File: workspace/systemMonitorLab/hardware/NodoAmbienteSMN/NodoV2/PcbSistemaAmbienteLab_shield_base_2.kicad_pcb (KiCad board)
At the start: 2 copper layers, 53.6 x 67.9 mm, 19 parts, among them J1 Molex_MainBoard_DHT22, J2 Molex_MainBoard_BMP280, J3 Molex_MainBoard_Led_Status, J4 DC 5V, Q1 NPN, Q2 NPN, Q3 NPN, U1 NodeMcuEsp8266

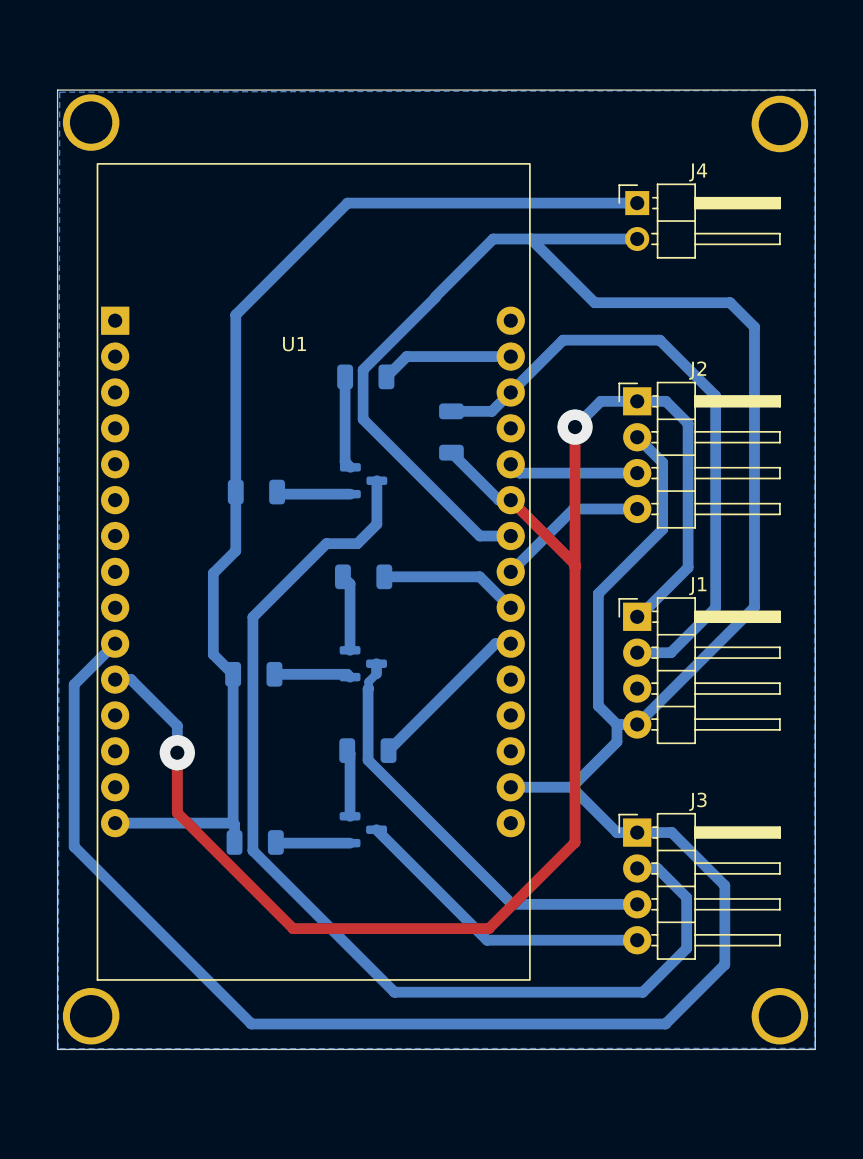
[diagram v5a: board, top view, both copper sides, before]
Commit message: Se termino de diseñar la version 2 del nodo ambiente, ahora se va a diseñar el case3d para que contenga al mismo
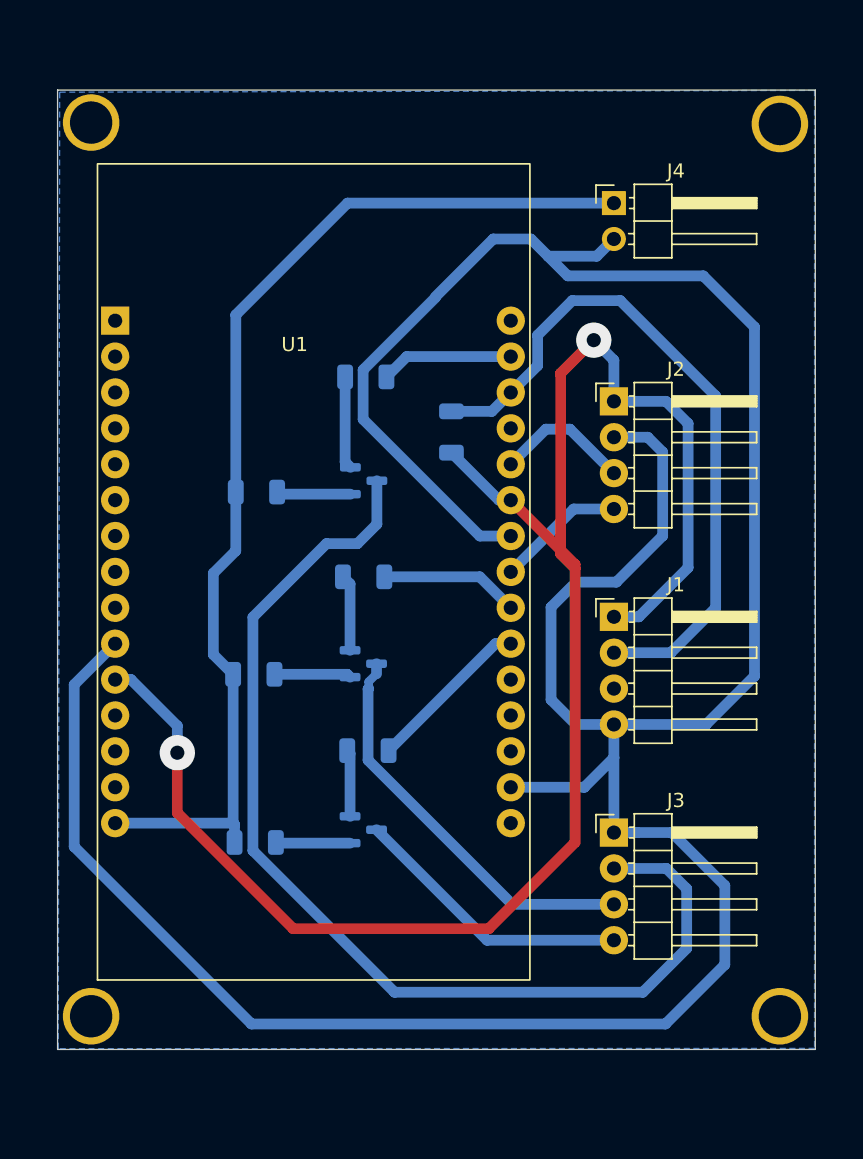
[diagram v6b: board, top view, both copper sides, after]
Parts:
- moved J1 1.65 mm to (156.2, 100.6)
- moved J2 1.65 mm to (156.2, 85.3)
- moved J3 1.65 mm to (156.2, 115.9)
- moved J4 1.65 mm to (156.2, 71.3)
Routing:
- net GND: track 214.1 -> 225.3 mm
- net 3V3: track 112.3 -> 122.9 mm
- net Net-(J1-Pin_2): track 44.3 -> 49.5 mm
- net Net-(J3-Pin_2): track 75.2 -> 77.2 mm
- net Net-(J3-Pin_3): track 30.4 -> 28.7 mm
- net Net-(J3-Pin_4): track 21.7 -> 20.0 mm
- net /shield_base/SDA: track 10.8 -> 9.14 mm
- net +5V: track 78.7 -> 77.0 mm

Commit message: Subo el resideño de los pcb's acorde al case 3d
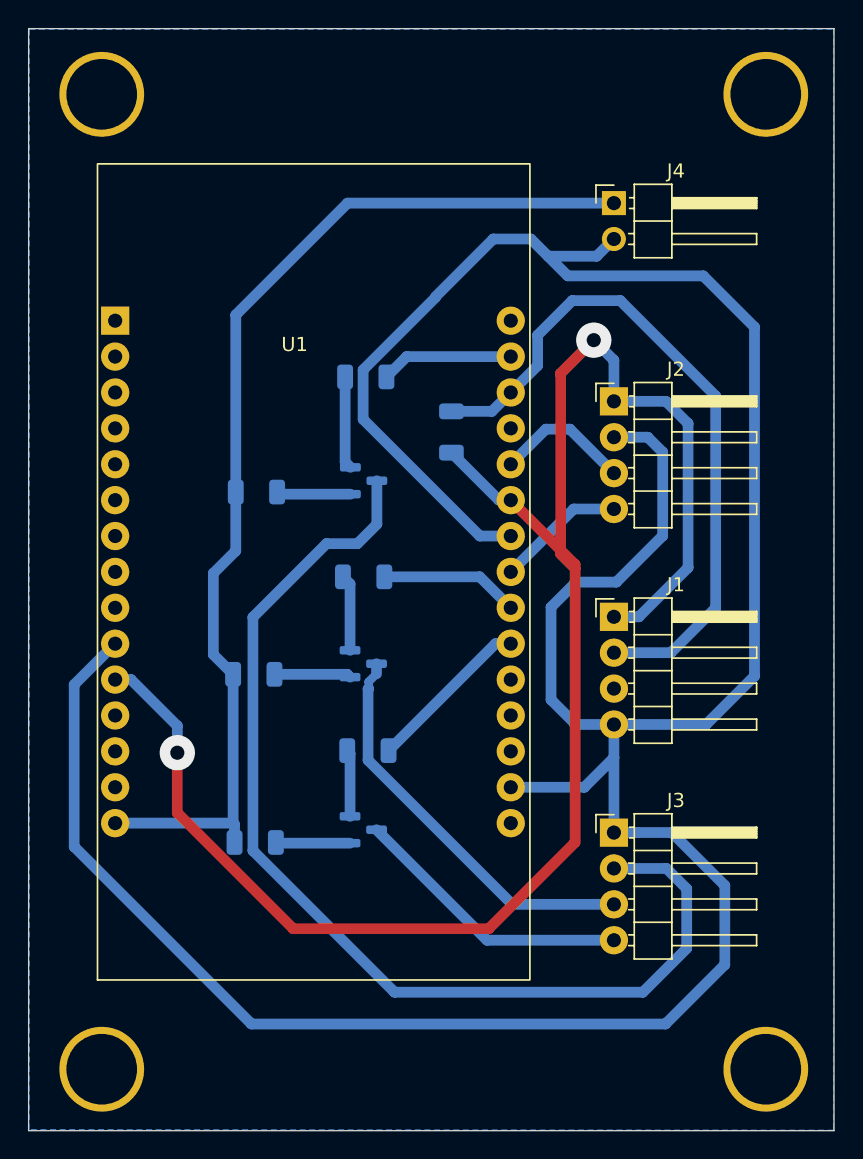
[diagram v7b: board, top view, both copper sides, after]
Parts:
- removed the ? at (117.3, 128.9)
- removed the ? at (168.1, 129.0)
- added ?: , , F.Cu at (121.1, 131.7)
- added ?: , , F.Cu at (168.1, 131.8)
- moved ? 1.41 mm to (167.1, 64.7)
- moved ? 1.00 mm to (118.2, 65.6)
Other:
- board size 53.6 x 67.9 mm -> 57 x 78 mm
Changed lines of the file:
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@@
 	(footprint ""
 		(layer "F.Cu")
-		(at 117.2 65.61)
+		(at 121.1 131.735)
 		(property "Reference" ""
 			(at 0 0 0)
@@
 		)
 		(pad "" thru_hole circle
-			(at 2 0 180)
-			(size 4 4)
-			(drill 3)
+			(at -1.15 0.875 180)
+			(size 6 6)
+			(drill 5)
+			(layers "*.Cu" "*.Mask")
+			(remove_unused_layers no)
+			(pinfunction "RV")
+			(pintype "bidirectional+no_connect")
+		)
+		(embedded_fonts no)
+	)
+	(footprint ""
+		(layer "F.Cu")
+		(at 118.2 65.61)
+		(property "Reference" ""
+			(at 0 0 0)
+			(layer "F.SilkS")
+			(effects
+				(font
+					(size 1.27 1.27)
+					(thickness 0.15)
+				)
+			)
+		)
+		(property "Value" ""
+			(at 0 0 0)
+			(layer "F.Fab")
+			(effects
+				(font
+					(size 1.27 1.27)
+					(thickness 0.15)
+				)
+			)
+		)
+		(property "Datasheet" ""
+			(at 0 0 0)
+			(layer "F.Fab")
+			(hide yes)
+			(effects
+				(font
+					(size 1.27 1.27)
+					(thickness 0.15)
+				)
+			)
+		)
+		(property "Description" ""
+			(at 0 0 0)
+			(layer "F.Fab")
+			(hide yes)
+			(effects
+				(font
+					(size 1.27 1.27)
+					(thickness 0.15)
+				)
+			)
+		)
+		(pad "" thru_hole circle
+			(at 1.75 -2 180)
+			(size 6 6)
+			(drill 5)
 			(layers "*.Cu" "*.Mask")
 			(remove_unused_layers no)
@@
 		(embedded_fonts no)
 	)
-	(footprint ""
-		(layer "F.Cu")
-		(at 117.3 128.86)
-		(property "Reference" ""
-			(at 0 0 0)
-			(layer "F.SilkS")
-			(effects
-				(font
-					(size 1.27 1.27)
-					(thickness 0.15)
-				)
-			)
-		)
-		(property "Value" ""
-			(at 0 0 0)
-			(layer "F.Fab")
-			(effects
-				(font
-					(size 1.27 1.27)
-					(thickness 0.15)
-				)
-			)
-		)
-		(property "Datasheet" ""
-			(at 0 0 0)
-			(layer "F.Fab")
-			(hide yes)
-			(effects
-				(font
-					(size 1.27 1.27)
-					(thickness 0.15)
-				)
-			)
-		)
-		(property "Description" ""
-			(at 0 0 0)
-			(layer "F.Fab")
-			(hide yes)
-			(effects
-				(font
-					(size 1.27 1.27)
-					(thickness 0.15)
-				)
-			)
-		)
-		(pad "" thru_hole circle
-			(at 1.9 0 180)
-			(size 4 4)
-			(drill 3)
-			(layers "*.Cu" "*.Mask")
-			(remove_unused_layers no)
-			(pinfunction "RV")
-			(pintype "bidirectional+no_connect")
-		)
-		(embedded_fonts no)
-	)
 	(footprint "Connector_PinHeader_2.54mm:PinHeader_1x04_P2.54mm_Horizontal"
 		(layer "F.Cu")
@@
 	(footprint ""
 		(layer "F.Cu")
-		(at 168.1 129.01)
+		(at 168.1 131.81)
 		(property "Reference" ""
 			(at 0 0 0)
@@
 		)
 		(pad "" thru_hole circle
-			(at -0.15 -0.15 180)
-			(size 4 4)
-			(drill 3)
+			(at -1.15 0.8 180)
+			(size 6 6)
+			(drill 5)
 			(layers "*.Cu" "*.Mask")
 			(remove_unused_layers no)
@@
 	(footprint ""
 		(layer "F.Cu")
-		(at 168.05 65.71 90)
+		(at 167.05 64.71 90)
 		(property "Reference" ""
 			(at 0 0 90)
@@
 		)
 		(pad "" thru_hole circle
-			(at 0 -0.1 270)
-			(size 4 4)
-			(drill 3)
+			(at 1.1 -0.1 270)
+			(size 6 6)
+			(drill 5)
 			(layers "*.Cu" "*.Mask")
 			(remove_unused_layers no)
@@
 	)
 	(gr_rect
-		(start 116.825 63.31)
-		(end 170.455 131.21)
+		(start 114.775 58.96)
+		(end 171.775 136.96)
 		(stroke
 			(width 0.05)
@@
 		(layer "Dwgs.User")
 		(pts
-			(xy 116.825 131.21) (xy 170.455 131.21)
+			(xy 171.775 58.96) (xy 171.775 136.96)
 		)
-		(height 4.8)
-		(orientation 0)
+		(height 18.48)
+		(orientation 1)
 		(format
 			(prefix "")
@@
 			(keep_text_aligned yes)
 		)
-		(gr_text "53.6300 mm"
-			(at 143.64 134.86 0)
+		(gr_text "78.0000 mm"
+			(at 189.105 97.96 90)
 			(layer "Dwgs.User")
 			(effects
@@
 		(layer "Dwgs.User")
 		(pts
-			(xy 170.45 63.36) (xy 170.35 131.21)
+			(xy 119.95 63.61) (xy 119.95 132.61)
 		)
-		(height 7.95)
+		(height -14.15)
 		(orientation 1)
 		(format
@@
 			(keep_text_aligned yes)
 		)
-		(gr_text "67.8500 mm"
-			(at 177.25 97.285 90)
+		(gr_text "69.0000 mm"
+			(at 104.65 98.11 90)
+			(layer "Dwgs.User")
+			(effects
+				(font
+					(size 1 1)
+					(thickness 0.15)
+				)
+			)
+		)
+	)
+	(dimension
+		(type orthogonal)
+		(layer "Dwgs.User")
+		(pts
+			(xy 114.775 59.235) (xy 171.775 59.235)
+		)
+		(height -7.315)
+		(orientation 0)
+		(format
+			(prefix "")
+			(suffix "")
+			(units 3)
+			(units_format 1)
+			(precision 4)
+		)
+		(style
+			(thickness 0.1)
+			(arrow_length 1.27)
+			(text_position_mode 0)
+			(arrow_direction outward)
+			(extension_height 0.58642)
+			(extension_offset 0.5)
+			(keep_text_aligned yes)
+		)
+		(gr_text "57.0000 mm"
+			(at 143.275 50.77 0)
+			(layer "Dwgs.User")
+			(effects
+				(font
+					(size 1 1)
+					(thickness 0.15)
+				)
+			)
+		)
+	)
+	(dimension
+		(type orthogonal)
+		(layer "Dwgs.User")
+		(pts
+			(xy 119.95 132.61) (xy 166.95 132.61)
+		)
+		(height 10.2)
+		(orientation 0)
+		(format
+			(prefix "")
+			(suffix "")
+			(units 3)
+			(units_format 1)
+			(precision 4)
+		)
+		(style
+			(thickness 0.1)
+			(arrow_length 1.27)
+			(text_position_mode 0)
+			(arrow_direction outward)
+			(extension_height 0.58642)
+			(extension_offset 0.5)
+			(keep_text_aligned yes)
+		)
+		(gr_text "47.0000 mm"
+			(at 143.45 141.66 0)
 			(layer "Dwgs.User")
 			(effects
@@
 		(filled_areas_thickness no)
 		(fill yes
-			(thermal_gap 0.25)
-			(thermal_bridge_width 2)
+			(thermal_gap 0.5)
+			(thermal_bridge_width 0.5)
 		)
 		(polygon
 			(pts
-				(xy 116.975 63.46) (xy 170.4 63.335) (xy 170.4 131.135) (xy 116.875 131.16)
+				(xy 114.825 59.01) (xy 171.75 58.985) (xy 171.75 136.935) (xy 114.8 136.885)
 			)
 		)

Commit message: Tareas Realizadas: 	- Se corrije la disposicion de los conectores, para que el cable 	  quede derecho en su construccion se tiene que invertir el 	  orden de los pines en las placas led_status y sensors. 	- Se Cambio el ancho de las pistas que atraviesan a los 	  resistores SMD de 30 a 25 mils. 	- Se esta transmitiendo al sevirdor nginx por el puerto 80. Tareas proximas: 	- Se debe Contruir las placas y realizar pruebas. 	- Modificar el firmware para que los led envien los estados por 	  PWM para el LED dual. y On - OFF para el Led simple. 	- Se debe agregar un filtro para que los datos que tengan una 	  varianza mayor a un valor x no se transmitan. 	- Se debe agregar un retardo para que no se transmitan los datos 	  de inicio del barometro, ya que siempre marcan un valor 	  alredeor de 700 hPa.
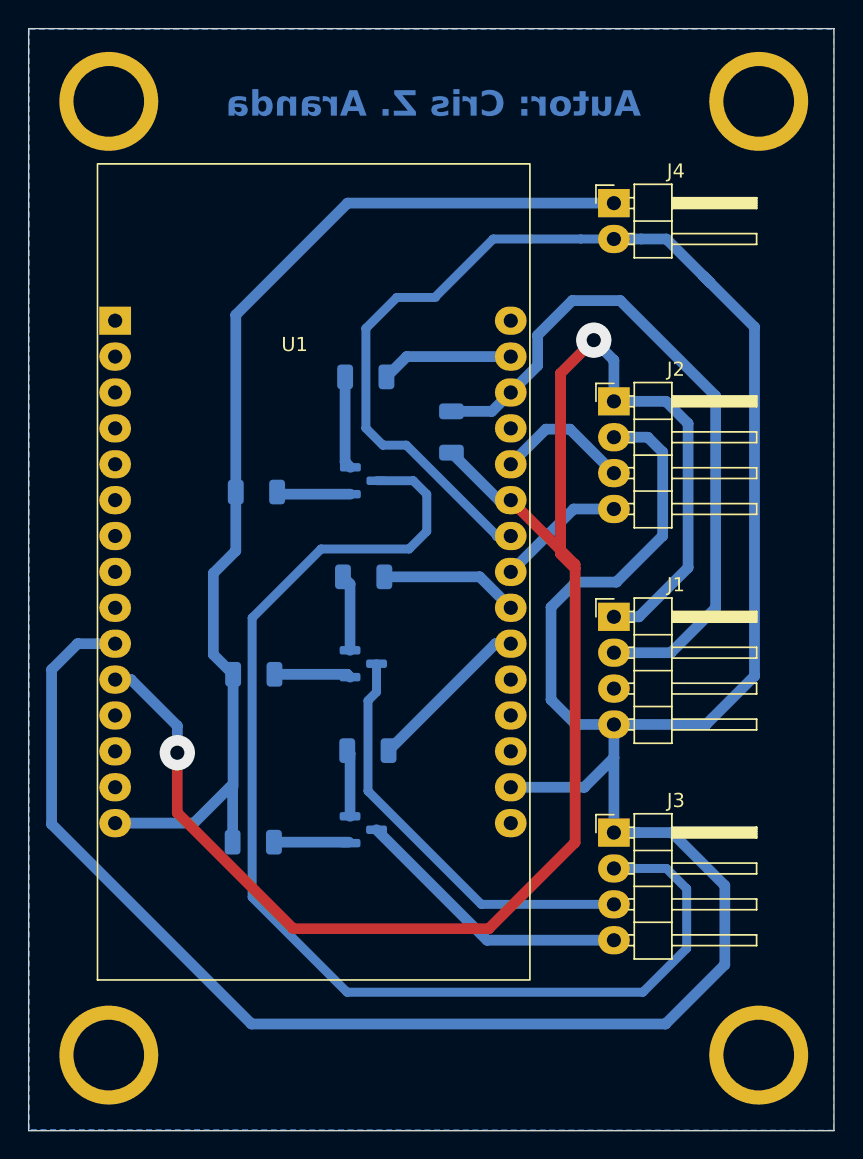
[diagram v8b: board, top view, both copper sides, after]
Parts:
- moved R6 0.14 mm to (130.7, 116.5)
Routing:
- net Net-(J3-Pin_2): track 77.2 -> 86.0 mm
- net Net-(J3-Pin_3): track 28.7 -> 30.0 mm
- net +5V: track 77.0 -> 78.2 mm
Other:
- board text added: "Autor: Cris Z. Aranda"
